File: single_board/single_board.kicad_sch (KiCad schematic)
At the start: 123 parts, among them J1 SWD, J11 SPI Debug, J17 BOOTSEL, J2 USB_C_Receptacle_USB2.0_16P, J3 RST, J30 JST_GH_H, J31 JST_GH_H, J32 PB_Vertical, J33 JST_GH_H, J34 PB_Vertical, J35 JST_GH_H, J36 JST_GH_H, J37 JST_GH_H, J38 PB_Vertical, J39 PB_Vertical, J40 PB_Vertical, J41 PB_Vertical, J42 PB_Vertical, J43 PB_Vertical, J44 PB_Vertical, J45 PB_Vertical, J46 PB_Vertical, J47 PB_Vertical, J48 PB_Vertical, J49 PB_Vertical, J5 JST-GH, J50 PB_Vertical, J6 Conn_01x02, Q1 AO3400A, Q3 AO3401A, SW1 Button, U1 AP2112K-3.3, U3 USBLC6-2SC6, U4 LSM6DSV, U5 STM32G474VBTx, Y1 FC-135

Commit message: Update footprints in project files
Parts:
- D3: footprint Rover:FM-B2020RGBA-HG Hand Solder -> rover:FM-B2020RGBA-HG Hand Solder
- Y1: footprint Rover:FC-135 Hand Solder -> rover:FC-135
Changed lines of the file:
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@@
 			)
 		)
-		(property "Footprint" "Rover:FM-B2020RGBA-HG Hand Solder"
+		(property "Footprint" "rover:FM-B2020RGBA-HG Hand Solder"
 			(at 431.8 387.35 0)
 			(hide yes)
@@
 			)
 		)
-		(property "Footprint" "Rover:FC-135 Hand Solder"
+		(property "Footprint" "rover:FC-135"
 			(at 337.82 349.25 0)
 			(hide yes)

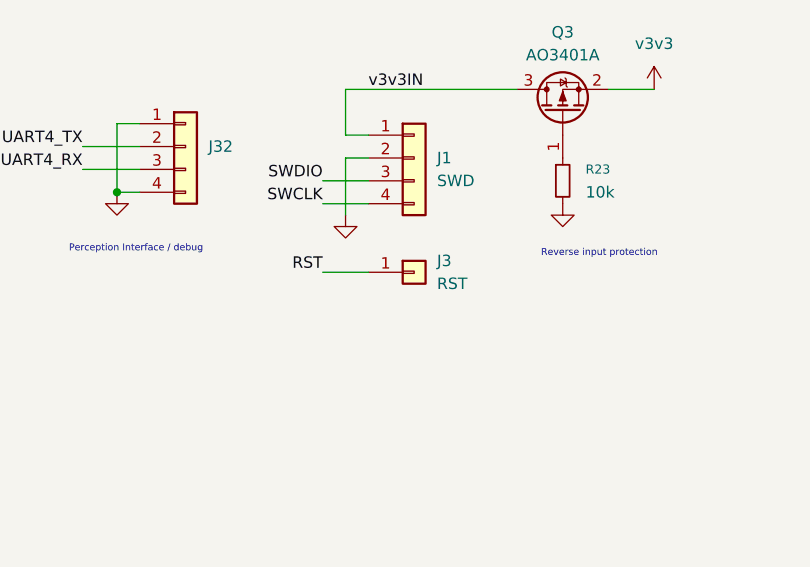
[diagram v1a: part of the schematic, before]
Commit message: Reset Pin to 1x02
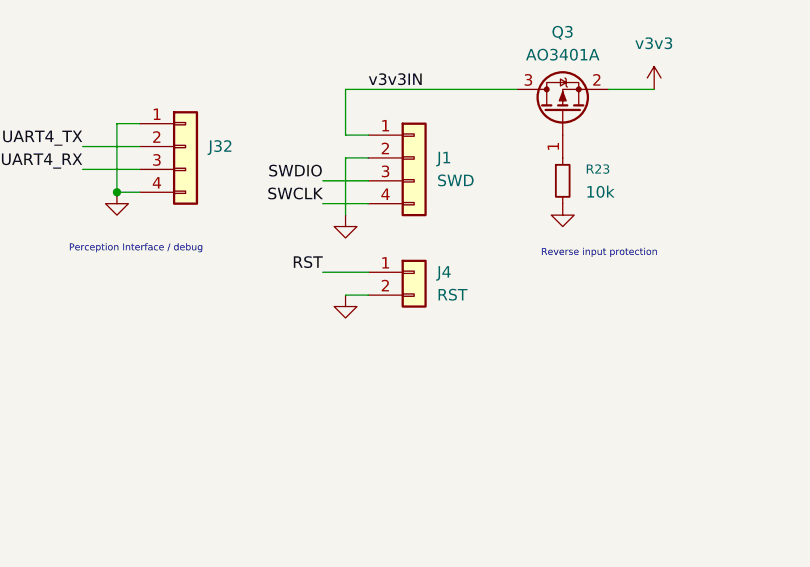
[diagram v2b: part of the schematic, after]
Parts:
- removed J3: RST, Connector_PinHeader_2.54mm:PinHeader_1x01_P2.54mm_Vertical, symbol Connector_Generic:Conn_01x01
- added J4: RST, Connector_PinHeader_2.54mm:PinHeader_1x02_P2.54mm_Vertical, symbol Connector_Generic:Conn_01x02
- D1: footprint Package_TO_SOT_SMD:SOT-23 -> rover:zener-3v6-onsemi-MMBZ5227BLT1G
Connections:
- net GND: now also J4.2 (Pin_2)
- net RST: now also J4.1 (Pin_1)
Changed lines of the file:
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@@
 	(wire
 		(pts
+			(xy 383.54 109.22) (xy 386.08 109.22)
+		)
+		(stroke
+			(width 0)
+			(type default)
+		)
+	)
+	(wire
+		(pts
 			(xy 287.02 220.98) (xy 300.99 220.98)
 		)
@@
 	(symbol
 		(lib_id "power:GND")
+		(at 383.54 109.22 0)
+		(mirror y)
+		(unit 1)
+		(body_style 1)
+		(exclude_from_sim no)
+		(in_bom yes)
+		(on_board yes)
+		(in_pos_files yes)
+		(dnp no)
+		(fields_autoplaced yes)
+		(property "Reference" "#PWR079"
+			(at 383.54 115.57 0)
+			(hide yes)
+			(show_name no)
+			(do_not_autoplace no)
+			(effects
+				(font
+					(size 1.27 1.27)
+				)
+			)
+		)
+		(property "Value" "GND"
+			(at 383.54 114.3 0)
+			(hide yes)
+			(show_name no)
+			(do_not_autoplace no)
+			(effects
+				(font
+					(size 1.27 1.27)
+				)
+			)
+		)
+		(property "Footprint" ""
+			(at 383.54 109.22 0)
+			(hide yes)
+			(show_name no)
+			(do_not_autoplace no)
+			(effects
+				(font
+					(size 1.27 1.27)
+				)
+			)
+		)
+		(property "Datasheet" ""
+			(at 383.54 109.22 0)
+			(hide yes)
+			(show_name no)
+			(do_not_autoplace no)
+			(effects
+				(font
+					(size 1.27 1.27)
+				)
+			)
+		)
+		(property "Description" "Power symbol creates a global label with name \"GND\" , ground"
+			(at 383.54 109.22 0)
+			(hide yes)
+			(show_name no)
+			(do_not_autoplace no)
+			(effects
+				(font
+					(size 1.27 1.27)
+				)
+			)
+		)
+		(pin "1"
+		)
+		(instances
+			(project "single_board"
+				(path "/ae10586e-ebf8-402d-a979-c2f011cdeee2"
+					(reference "#PWR079")
+					(unit 1)
+				)
+			)
+		)
+	)
+	(symbol
+		(lib_id "power:GND")
 		(at 430.53 340.36 0)
 		(mirror y)
@@
 	)
 	(symbol
-		(lib_id "Connector_Generic:Conn_01x01")
-		(at 391.16 106.68 0)
-		(unit 1)
-		(body_style 1)
-		(exclude_from_sim no)
-		(in_bom yes)
-		(on_board yes)
-		(in_pos_files yes)
-		(dnp no)
-		(fields_autoplaced yes)
-		(property "Reference" "J3"
-			(at 393.7 105.4099 0)
-			(show_name no)
-			(do_not_autoplace no)
-			(effects
-				(font
-					(size 1.27 1.27)
-				)
-				(justify left)
-			)
-		)
-		(property "Value" "RST"
-			(at 393.7 107.9499 0)
-			(show_name no)
-			(do_not_autoplace no)
-			(effects
-				(font
-					(size 1.27 1.27)
-				)
-				(justify left)
-			)
-		)
-		(property "Footprint" "Connector_PinHeader_2.54mm:PinHeader_1x01_P2.54mm_Vertical"
-			(at 391.16 106.68 0)
-			(hide yes)
-			(show_name no)
-			(do_not_autoplace no)
-			(effects
-				(font
-					(size 1.27 1.27)
-				)
-			)
-		)
-		(property "Datasheet" ""
-			(at 391.16 106.68 0)
-			(hide yes)
-			(show_name no)
-			(do_not_autoplace no)
-			(effects
-				(font
-					(size 1.27 1.27)
-				)
-			)
-		)
-		(property "Description" "Generic connector, single row, 01x01, script generated (kicad-library-utils/schlib/autogen/connector/)"
-			(at 391.16 106.68 0)
-			(hide yes)
-			(show_name no)
-			(do_not_autoplace no)
-			(effects
-				(font
-					(size 1.27 1.27)
-				)
-			)
-		)
-		(pin "1"
-		)
-		(instances
-			(project "single_board"
-				(path "/ae10586e-ebf8-402d-a979-c2f011cdeee2"
-					(reference "J3")
-					(unit 1)
-				)
-			)
-		)
-	)
-	(symbol
 		(lib_id "power:GND")
 		(at 240.03 254 0)
@@
 	)
 	(symbol
+		(lib_id "Connector_Generic:Conn_01x02")
+		(at 391.16 106.68 0)
+		(unit 1)
+		(body_style 1)
+		(exclude_from_sim no)
+		(in_bom yes)
+		(on_board yes)
+		(in_pos_files yes)
+		(dnp no)
+		(fields_autoplaced yes)
+		(property "Reference" "J4"
+			(at 393.7 106.6799 0)
+			(show_name no)
+			(do_not_autoplace no)
+			(effects
+				(font
+					(size 1.27 1.27)
+				)
+				(justify left)
+			)
+		)
+		(property "Value" "RST"
+			(at 393.7 109.2199 0)
+			(show_name no)
+			(do_not_autoplace no)
+			(effects
+				(font
+					(size 1.27 1.27)
+				)
+				(justify left)
+			)
+		)
+		(property "Footprint" "Connector_PinHeader_2.54mm:PinHeader_1x02_P2.54mm_Vertical"
+			(at 391.16 106.68 0)
+			(hide yes)
+			(show_name no)
+			(do_not_autoplace no)
+			(effects
+				(font
+					(size 1.27 1.27)
+				)
+			)
+		)
+		(property "Datasheet" ""
+			(at 391.16 106.68 0)
+			(hide yes)
+			(show_name no)
+			(do_not_autoplace no)
+			(effects
+				(font
+					(size 1.27 1.27)
+				)
+			)
+		)
+		(property "Description" "Generic connector, single row, 01x02, script generated (kicad-library-utils/schlib/autogen/connector/)"
+			(at 391.16 106.68 0)
+			(hide yes)
+			(show_name no)
+			(do_not_autoplace no)
+			(effects
+				(font
+					(size 1.27 1.27)
+				)
+			)
+		)
+		(pin "2"
+		)
+		(pin "1"
+		)
+		(instances
+			(project "single_board"
+				(path "/ae10586e-ebf8-402d-a979-c2f011cdeee2"
+					(reference "J4")
+					(unit 1)
+				)
+			)
+		)
+	)
+	(symbol
 		(lib_id "power:GND")
 		(at 170.18 237.49 0)
@@
 			)
 		)
-		(property "Footprint" "Package_TO_SOT_SMD:SOT-23"
+		(property "Footprint" "rover:zener-3v6-onsemi-MMBZ5227BLT1G"
 			(at 40.64 36.83 90)
 			(hide yes)

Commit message: Schematic Changes
HSE 16 MHz
Major Pinout Change
Fix 5V LDO jumper topology
Change Mode LED
Encoder type split
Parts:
- removed C32, C33: 10pF, Capacitor_SMD:C_0402_1005Metric, symbol Device:C_Small
- removed D3: FM-B2020RGBA-HG, rover:FM-B2020RGBA-HG Hand Solder, symbol Device:LED_RBAG
- removed Y1: FC-135, rover:FC-135, symbol Device:Crystal
- added D5: TJ-S1615CY6TGLCCSRGB-A5, rover:TOGAILED, symbol Device:LED_KBRG
- added Y2: ABM8-16MHz, Crystal:Crystal_SMD_Abracon_ABM8G-4Pin_3.2x2.5mm, symbol Device:Crystal_GND24_Small
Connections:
- net OSC32_IN is gone; now on net LIM_SW2: U5.8 (PC14)
- net OSC32_OUT is gone; now on net LIM_SW3: U5.9 (PC15)
- net VBUS is gone; now on net 5V: C11.1, J2.A4 (VBUS), J2.A9 (VBUS), J2.B4 (VBUS), J2.B9 (VBUS), J6.2 (Pin_2), U3.5 (VBUS)
- net 5V: now also J39.1 (Pin_1), J40.1 (Pin_1), J41.1 (Pin_1), J42.1 (Pin_1), J43.1 (Pin_1), J44.1 (Pin_1); no longer C3.1, C31.1, C4.1, J39.3 (Pin_3), J40.3 (Pin_3), J41.3 (Pin_3), J42.3 (Pin_3), J43.3 (Pin_3), J44.3 (Pin_3), J6.1 (Pin_1), U1.1 (VIN), U1.3 (EN)
- net CAN_LED: now also U5.58 (PD11); no longer U5.54 (PB15)
- net CAN_RX: now also U5.82 (PD0); no longer U5.51 (PB12)
- net CAN_STB: now also U5.84 (PD2); no longer U5.53 (PB14)
- net CAN_TX: now also U5.83 (PD1); no longer U5.52 (PB13)
- net DIR1: now also U5.90 (PB3); no longer U5.18 (PC3)
- net DIR2: now also U5.96 (PB9); no longer U5.26 (PA4)
- net DIR3: now also U5.4 (PE5); no longer U5.5 (PE6)
- net DIR4: now also U5.18 (PC3); no longer U5.68 (PC9)
- net DIR5: now also U5.19 (PF2); no longer U5.61 (PD14)
- net DIR6: now also U5.26 (PA4); no longer U5.97 (PE0)
- net ENC1_A: now also J39.2 (Pin_2), U5.91 (PB4); no longer J39.1 (Pin_1), U5.15 (PC0)
- net ENC1_B: now also J39.3 (Pin_3), U5.92 (PB5); no longer J39.2 (Pin_2), U5.16 (PC1)
- net ENC2_A: now also J40.2 (Pin_2), U5.93 (PB6); no longer J40.1 (Pin_1), U5.20 (PA0)
- net ENC2_B: now also J40.3 (Pin_3), U5.94 (PB7); no longer J40.2 (Pin_2), U5.21 (PA1)
- net ENC3_A: now also J41.2 (Pin_2), U5.1 (PE2); no longer J41.1 (Pin_1), U5.28 (PA6)
- net ENC3_B: now also J41.3 (Pin_3), U5.2 (PE3); no longer J41.2 (Pin_2), U5.29 (PA7)
- net ENC4_A: now also J42.2 (Pin_2), U5.15 (PC0); no longer J42.1 (Pin_1), U5.59 (PD12)
- net ENC4_B: now also J42.3 (Pin_3), U5.16 (PC1); no longer J42.2 (Pin_2), U5.60 (PD13)
- net GND: now also J43.3 (Pin_3), J44.3 (Pin_3), D5.1 (K), Y2.2 (G), Y2.4 (G); no longer J43.4 (Pin_4), J44.4 (Pin_4)
- net HEARTBEAT: now also U5.57 (PD10); no longer U5.55 (PD8)
- net I2C_SCL: now also U5.69 (PA8); no longer U5.70 (PA9)
- net I2C_SDA: now also U5.68 (PC9); no longer U5.69 (PA8)
- net IMU_MISO: now also U5.28 (PA6); no longer U5.91 (PB4)
- net IMU_MOSI: now also U5.29 (PA7); no longer U5.92 (PB5)
- net IMU_NSS: now also U5.30 (PC4); no longer U5.89 (PD7)
- net IMU_SCK: now also U5.27 (PA5); no longer U5.90 (PB3)
- net INT1: now also U5.31 (PC5); no longer U5.93 (PB6)
- net INT2: now also U5.32 (PB0); no longer U5.88 (PD6)
- net LASER_SIG: now also U5.43 (PE12); no longer U5.46 (PE15)
- net LED1: now also U5.56 (PD9); no longer U5.27 (PA5)
- net LED2: now also U5.55 (PD8); no longer U5.30 (PC4)
- net LED3: now also U5.54 (PB15); no longer U5.31 (PC5)
- net LED4: now also U5.53 (PB14); no longer U5.32 (PB0)
- net LED5: now also U5.52 (PB13); no longer U5.33 (PB1)
- net LED6: now also U5.51 (PB12); no longer U5.34 (PB2)
- net LIM_SW1: now also U5.7 (PC13); no longer U5.43 (PE12)
- net LIM_SW2: no longer U5.44 (PE13)
- net LIM_SW3: no longer U5.45 (PE14)
- net PWM1: now also U5.97 (PE0); no longer U5.17 (PC2)
- net PWM2: now also U5.98 (PE1); no longer U5.25 (PA3)
- net PWM3: now also U5.3 (PE4); no longer U5.4 (PE5)
- net PWM4: now also U5.17 (PC2); no longer U5.67 (PC8)
- net PWM5: now also U5.22 (PA2); no longer U5.62 (PD15)
- net PWM6: now also U5.25 (PA3); no longer U5.98 (PE1)
- net TRI_LED_B: now also R3.1, U5.67 (PC8); no longer R9.2, U5.87 (PD5)
- net TRI_LED_G: now also R7.1, U5.65 (PC6); no longer R7.2, U5.85 (PD3)
- net TRI_LED_R: now also R9.1, U5.66 (PC7); no longer R3.2, U5.86 (PD4)
- net OSC_IN: now reaches U5.12 (PF0)
- net OSC_IN: now also Y2.1
- net OSC_OUT: now reaches U5.13 (PF1)
- net OSC_OUT: now also Y2.3
- net USART3_TX: now reaches U5.47 (PB10)
- net USART3_TX: now also J5.3 (Pin_3)
- net USART1_RX: now reaches U5.71 (PA10)
- net USART1_RX: now also J32.3 (Pin_3)
- removed net ENC5_A: J43.1 (Pin_1), U5.65 (PC6)
- net ENC5_B renamed ENC5
- net ENC5: no longer U5.66 (PC7)
- removed net ENC6_A: J44.1 (Pin_1), U5.1 (PE2)
- net ENC6_B renamed ENC_6
- net ENC_6: now also U5.21 (PA1); no longer U5.2 (PE3)
- net UART4_RX: no longer names the net of U5.80 (PC11)
- net UART4_RX: no longer J32.3 (Pin_3)
- net UART4_TX: no longer names the net of U5.79 (PC10)
- net UART4_TX: no longer J32.2 (Pin_2)
- net UART5_RX renamed USART3_RX
- net USART3_RX: now also U5.46 (PE15); no longer U5.84 (PD2)
- net UART5_TX: no longer names the net of U5.81 (PC12)
- net UART5_TX: no longer J5.3 (Pin_3)
- new net: C3.1, C31.1, C4.1, J6.1 (Pin_1), U1.1 (VIN), U1.3 (EN)
- new net: D5.4 (GA), R7.2
- new net: D5.3 (RA), R9.2
- new net: D5.2 (BA), R3.2
- new net ENC_5: U5.20 (PA0)
- new net USART1_TX: J32.2 (Pin_2), U5.70 (PA9)
- no-connect marks 40 -> 41
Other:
- note added: "---TIM1_CH3"
- note added: "---TIM2_CH1 PWM Input"
- note added: "---TIM2_CH3"
- note added: "---TIM2_CH4"
- note added: "---TIM5_CH2 PWM Input"
- note added: "1 for each motor set"
- note added: "5V to LDO Jumper Bridge if using USB"
- note added: "===TIM1 Encoder Mode"
- note added: "===TIM3 Encoder Mode"
- note added: "===TIM4 Encoder Mode"
- note added: "===TIM8_CH1-CH3 PWM Generate"
- note added: "ADC3 IN14---"
- note added: "ENC1-ENC4: Quadrature mode Pin setup: Encoder mode TIMx_CH1 and CH2 (can be reconfigured to PWM input for Absolute mode)"
- note added: "ENC5-ENC6 / ABS_5-ABS_6: Absolute mode (PWM duty cycle) Pin setup: PWM input (takes 2 channels) !! Cannot be reconfigured for Quadrature mode. !! Reserved for arm joints restricted to <360 degrees"
- note added: "I2C3"
- note added: "Motor Controls"
- note added: "TIM16_CH1---"
- note added: "TIM20 Encoder Mode==="
- note added: "TIM20_CH4---"
- note added: "TIM3_CH3---"
- note added: "async"
- note removed: "5V to LDO Jumper Bridge if using USB or ST-Link 5V"
- note removed: "Analog, ADC3 IN14"
- note removed: "Encoders for DC Motors: Pin Arrangement for absolute encoder (ENC_B to PWM input) Optional ENC_A for quadrature"
- note removed: "Encoders for Stepper Motors: Pin Arrangement for quadrature encoder Deactivate ENC1_A for absolute"
- note removed: "For example: indicate encoder/motor direction; Verify or characterize that software, signal, and hardware all behave as expected"
- note removed: "MCU spec section 5.3.7 R_ext is not needed for OSC32"
- note removed: "MODE LED"
- note removed: "Motors"
- note removed: "ST AN2867 - Seiko Epson - 7pf model; Digikey PCB Routing also based on A.N."
- note removed: "TIM1 CH1,2 PWM read"
- note removed: "TIM1 CH3, PWM generate"
- note removed: "TIM2 CH1,2 PWM read"
- note removed: "TIM2 CH4, PWM generate"
- note removed: "TIM20 CH1,2 PWM read"
- note removed: "TIM20 CH4, PWM generate"
- note removed: "TIM3 CH1,2 PWM read"
- note removed: "TIM3 CH4, PWM generate"
- note removed: "TIM4 CH1,2 PWM read"
- note removed: "TIM4 CH4, PWM generate"
- note removed: "TIM8 CH1,2 PWM read"
- note removed: "TIM8 CH3, PWM generate"
- note removed: "mcu spec 100nf on reset per datasheet see 5.3.15"
- note removed: "vbus spec max capacitance 10uF"
- moved on the sheet: C11, C12, C13, C14, C15, C16, C17, C18, C19, C20, C21, C22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

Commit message: layout positioning
spacing and positioning
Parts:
- removed J1: SWD, Connector_PinHeader_2.54mm:PinHeader_1x04_P2.54mm_Vertical, symbol Connector_Generic:Conn_01x04
- removed J4: RST, Connector_PinHeader_2.54mm:PinHeader_1x02_P2.54mm_Vertical, symbol Connector_Generic:Conn_01x02
- added C35, C36: 10pF, Capacitor_SMD:C_0402_1005Metric, symbol Device:C_Small
- added J3: SWD, Connector_PinHeader_2.54mm:PinHeader_1x05_P2.54mm_Vertical, symbol Connector_Generic:Conn_01x05
- J32: value PB_Vertical -> (none); footprint Connector_Molex:Molex_PicoBlade_53047-0410_1x04_P1.25mm_Vertical -> Connector_PinHeader_2.54mm:PinHeader_1x04_P2.54mm_Vertical
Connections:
- net ENC5 is gone; now on net ENC_5: J43.2 (Pin_2)
- net 5V: now also D2.2 (A); no longer R14.1
- net ENC_5: now also U5.21 (PA1); no longer U5.20 (PA0)
- net ENC_6: now also U5.20 (PA0); no longer U5.21 (PA1)
- net GND: now also R14.2, R15.2, C35.2, C36.2, J3.2 (Pin_2); no longer D2.1 (K), D4.1 (K)
- net LASER_SIG: now also U5.42 (PE11); no longer U5.43 (PE12)
- net LIM_SW1: now also U5.43 (PE12); no longer U5.7 (PC13)
- net LIM_SW2: now also U5.44 (PE13); no longer U5.8 (PC14)
- net LIM_SW3: now also U5.45 (PE14); no longer U5.9 (PC15)
- net OSC_IN: now also C36.1
- net OSC_OUT: now also C35.1
- net RST: now also J3.5 (Pin_5)
- net SWCLK: now also J3.4 (Pin_4)
- net SWDIO: now also J3.3 (Pin_3)
- net USART3_RX: now also U5.80 (PC11); no longer U5.46 (PE15)
- net USART3_TX: now also U5.79 (PC10); no longer U5.47 (PB10)
- net v3v3: now also D4.2 (A); no longer R15.1
- net v3v3IN: now also J3.1 (Pin_1)
- new net: D2.1 (K), R14.1
- new net: D4.1 (K), R15.1
- no-connect marks 41 -> 36
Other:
- moved on the sheet: D2, D4, R14, R15

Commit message: LDO Power Jumper
Improved topology and usability
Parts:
- removed J32: (no value), Connector_PinHeader_2.54mm:PinHeader_1x04_P2.54mm_Vertical, symbol Connector_Generic:Conn_01x04
- removed J6: Conn_01x02, Connector_PinHeader_2.54mm:PinHeader_1x02_P2.54mm_Vertical, symbol Connector_Generic:Conn_01x02
- added J18: Power, Connector_PinHeader_2.54mm:PinHeader_1x03_P2.54mm_Vertical, symbol Connector_Generic:Conn_01x03
- added J52: (no value), Connector_PinHeader_2.54mm:PinHeader_1x04_P2.54mm_Vertical, symbol Connector_Generic:Conn_01x04
- added J53: PB_Vertical, Connector_Molex:Molex_PicoBlade_53047-0410_1x04_P1.25mm_Vertical, symbol Connector_Generic:Conn_01x04
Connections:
- net 5V: now also J18.1 (Pin_1)
- net GND: now also J52.1 (Pin_1), J52.4 (Pin_4), J53.1 (Pin_1), J53.4 (Pin_4)
- net USART1_RX: now also J53.3 (Pin_3)
- net USART1_TX: now also J53.2 (Pin_2)
- net USART3_RX: now also J52.3 (Pin_3); no longer J5.4 (Pin_4)
- net USART3_TX: now also J52.2 (Pin_2); no longer J5.3 (Pin_3)
- net at C3.1, C31.1, C4.1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: now also J18.2 (Pin_2)
- net USART2_TX: now reaches U5.87 (PD5)
- net USART2_TX: now also J5.3 (Pin_3)
- net USART2_RX: now reaches U5.88 (PD6)
- net USART2_RX: now also J5.4 (Pin_4)
- no-connect marks 36 -> 35
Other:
- note added: "UART / GPIO for Perception and Science Interface"
- note removed: "Perception Interface / debug"

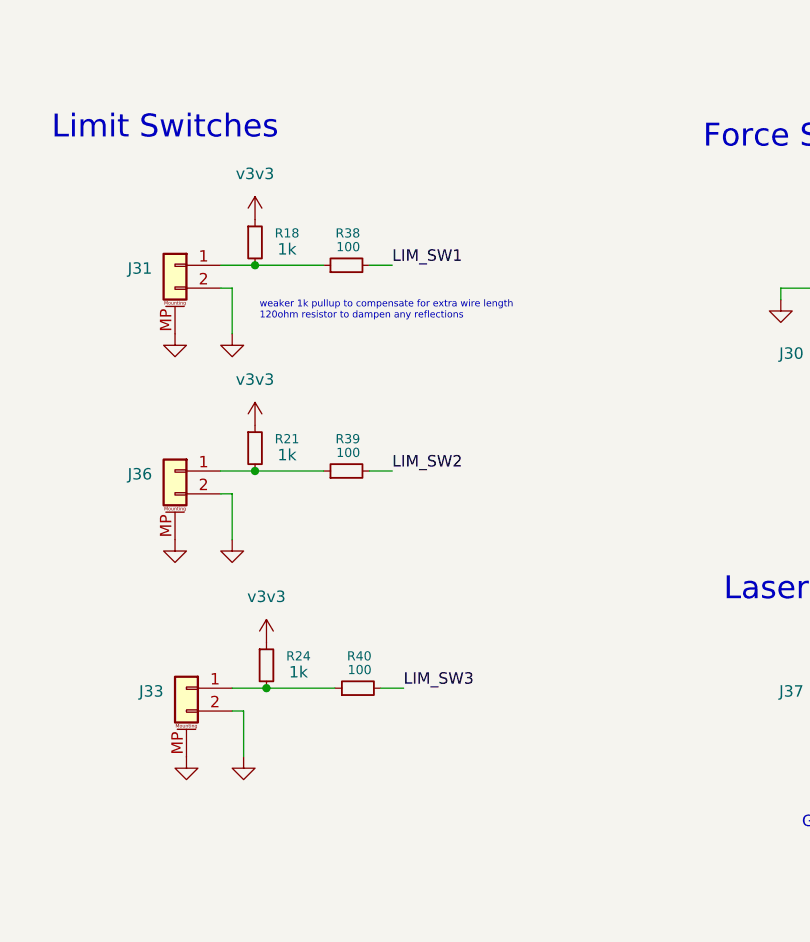
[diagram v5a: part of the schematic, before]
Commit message: Limit switch topology
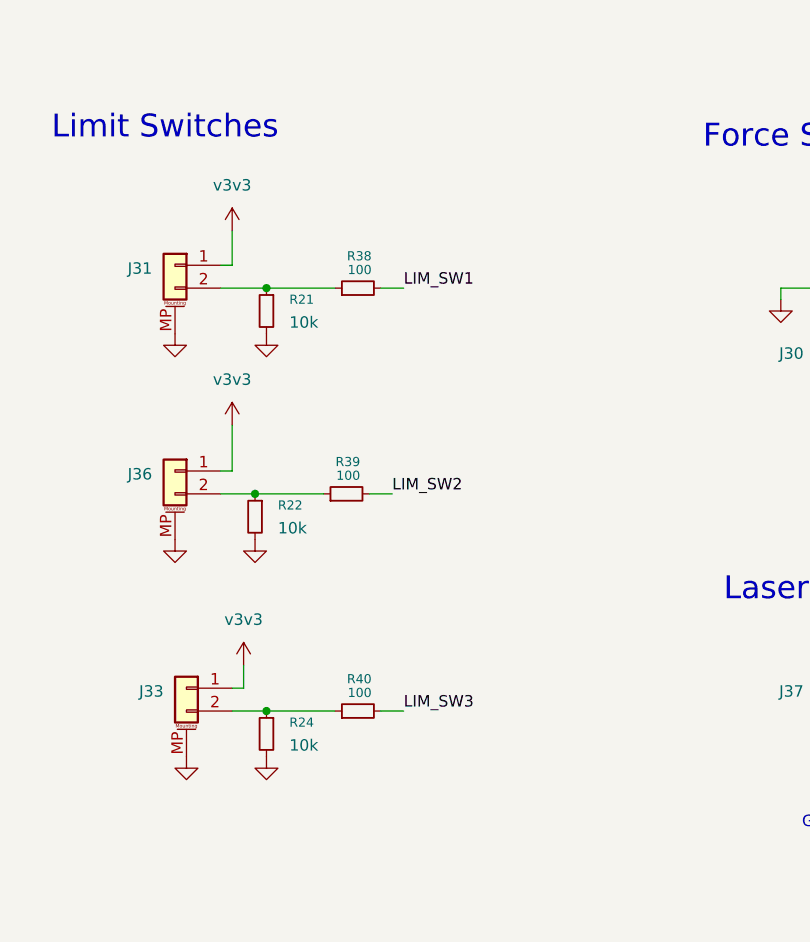
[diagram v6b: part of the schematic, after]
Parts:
- removed R18: 1k, Resistor_SMD:R_0402_1005Metric, symbol Device:R_Small
- added R22: 10k, Resistor_SMD:R_0402_1005Metric, symbol Device:R_Small
- R21, R24: value 1k -> 10k
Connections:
- net GND: now also R21.2, R24.2, R22.2; no longer J31.2 (Pin_2), J33.2 (Pin_2), J36.2 (Pin_2)
- net v3v3: now also J31.1 (Pin_1), J33.1 (Pin_1), J36.1 (Pin_1); no longer R21.1, R24.1
- net at R38.1: now also J31.2 (Pin_2), R21.1; no longer J31.1 (Pin_1)
- new net: J36.2 (Pin_2), R22.1, R39.1
- new net: J33.2 (Pin_2), R24.1, R40.1
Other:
- note removed: "weaker 1k pullup to compensate for extra wire length 120ohm resistor to dampen any reflections"
- moved on the sheet: R38, R39, R40

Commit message: Tri color LED resistors
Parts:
- removed R3, R7, R9: 1k, Resistor_SMD:R_0402_1005Metric, symbol Device:R_Small
- added R10: 10k, Resistor_SMD:R_0402_1005Metric, symbol Device:R_Small
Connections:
- net GND: now also R10.2; no longer D5.1 (K)
- net TRI_LED_B: now also D5.2 (BA)
- net TRI_LED_G: now also D5.4 (GA)
- net TRI_LED_R: now also D5.3 (RA)
- new net: D5.1 (K), R10.1
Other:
- moved on the sheet: J33, J36, R22, R24, R39, R40
